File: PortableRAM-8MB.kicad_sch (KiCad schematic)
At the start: 34 parts, among them J1 RAM Connector, J2 JTAG_Header_2.54mm_1x06, U1 ATF1502ASL, U10 AMS1117-3.3, U11 74HC245, U12 74HC245, U2 IS61WV5128BLL-10TLI, U3 IS61WV5128BLL-10TLI, U4 IS61WV5128BLL-10TLI, U5 IS61WV5128BLL-10TLI, U6 IS61WV5128BLL-10TLI, U7 IS61WV5128BLL-10TLI, U8 IS61WV5128BLL-10TLI, U9 IS61WV5128BLL-10TLI

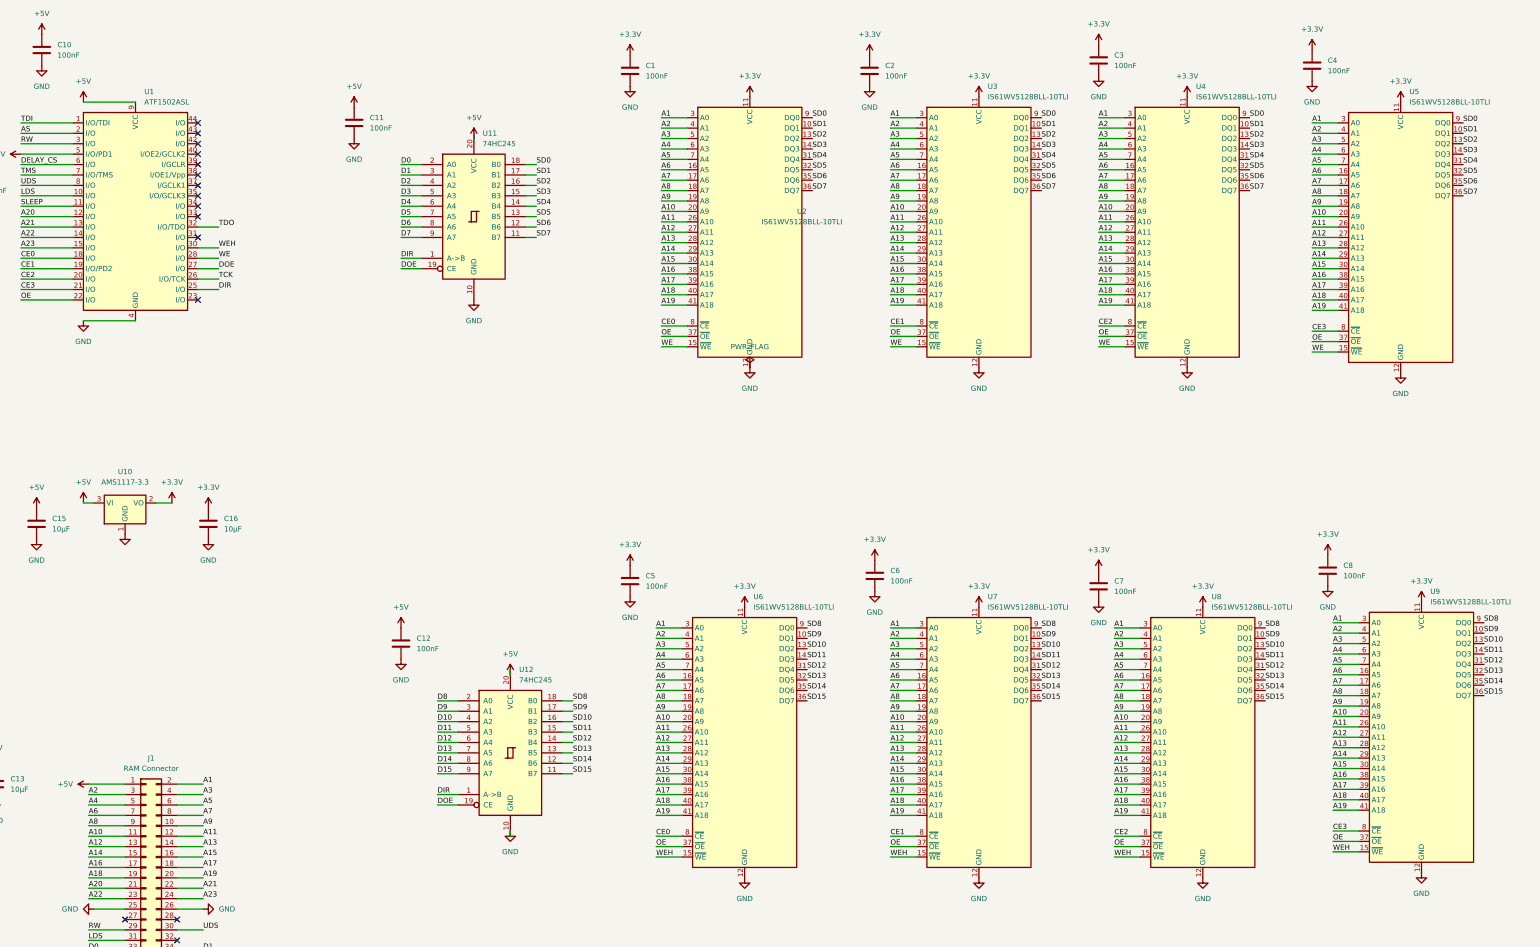
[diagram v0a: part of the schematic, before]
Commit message: Schematic: all-5V conversion + AS6C8008 (1Mx8) memory swap
- All +3.3V power symbols converted to +5V; AMS1117 LDO (U10) and its
  rail markers/stub wires removed — single 5V domain
- SRAM symbol renumbered in place to the AS6C8008 TSOP-II-44 pinout
  (graphics, wires, and labels untouched); pins 33/34 kept as VCC/GND
  rail ties (NC on the chip, preserves board plane stitching)
- New pins: A19 (18) labeled A19RAM on all 8 chips, driven by CPLD
  pin 33; CE2 (40) tied to +5V via power symbols
- PortableRAM.kicad_sym updated: AS6C8008 replaces IS61WV5128BLL
- ERC: no new issues vs v0.2 baseline (PWR_FLAG/VCC-alias warnings
  and prior exclusions remain)

Co-Authored-By: Claude Fable 5 <noreply@anthropic.com>
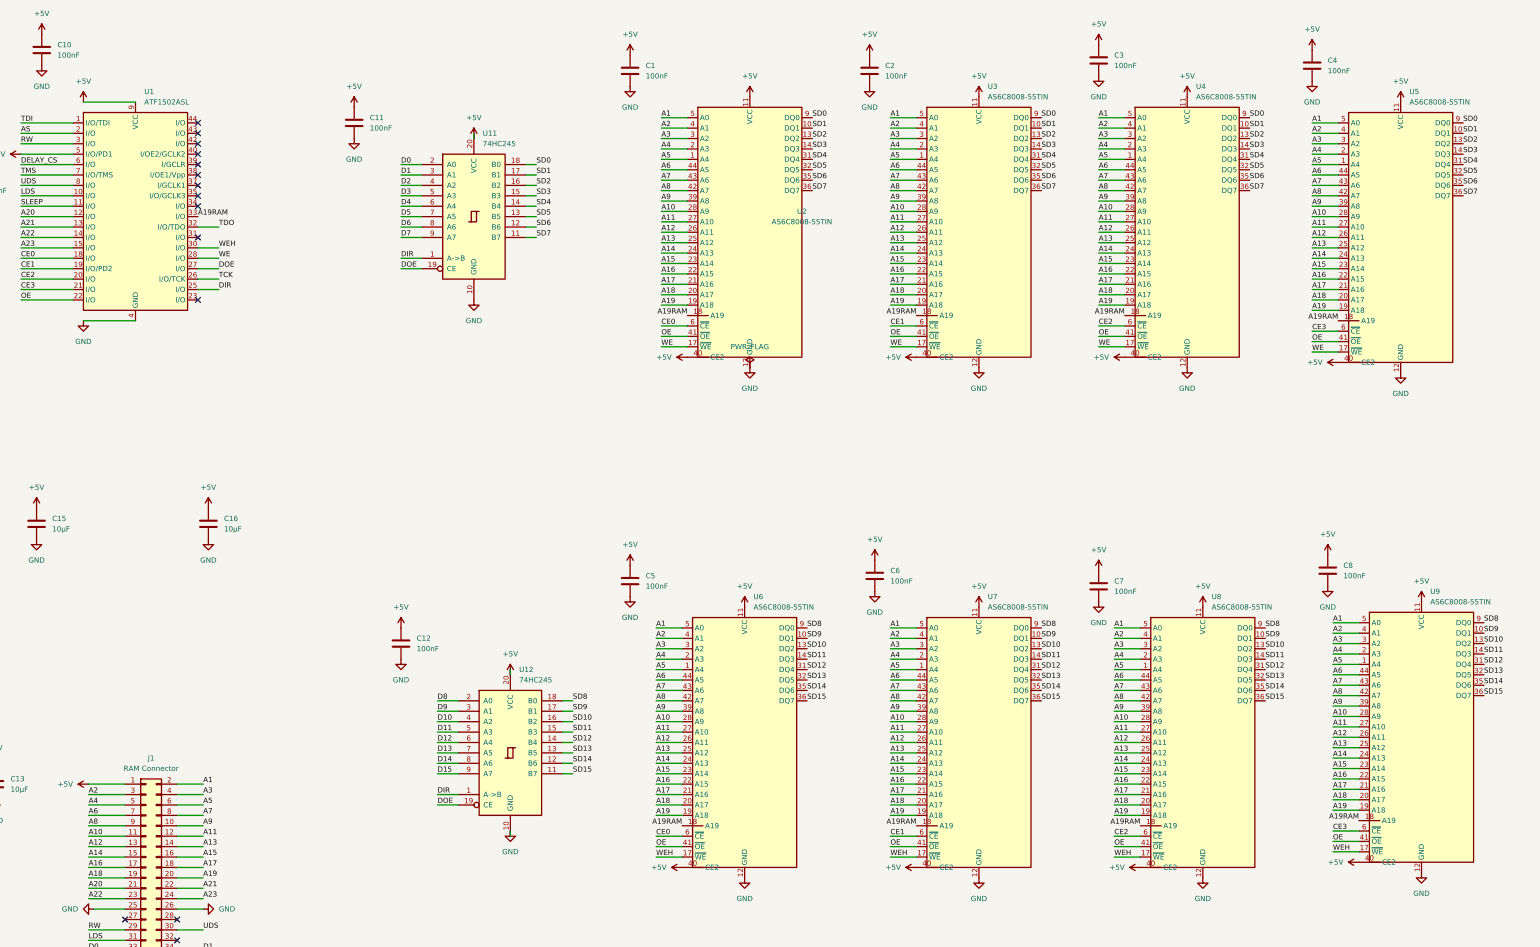
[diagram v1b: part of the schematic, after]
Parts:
- removed U10: AMS1117-3.3, Package_TO_SOT_SMD:SOT-223-3_TabPin2, symbol Regulator_Linear:AMS1117-3.3
- U2, U3, U4, U5, U6, U7, U8, U9: value IS61WV5128BLL-10TLI -> AS6C8008-55TIN; symbol PortableRAM:IS61WV5128BLL -> PortableRAM:AS6C8008
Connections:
- net +3.3V is gone; now on net +5V: C1.1, C16.1, C2.1, C3.1, C4.1, C5.1, C6.1, C7.1, C8.1, U2.11 (VCC), U2.33 (VCC), U3.11 (VCC), U3.33 (VCC), U4.11 (VCC), U4.33 (VCC), U5.11 (VCC), U5.33 (VCC), U6.11 (VCC), U6.33 (VCC), U7.11 (VCC), U7.33 (VCC), U8.11 (VCC), U8.33 (VCC), U9.11 (VCC), U9.33 (VCC)
- net +5V: now also U2.40 (CE2), U3.40 (CE2), U4.40 (CE2), U5.40 (CE2), U6.40 (CE2), U7.40 (CE2), U8.40 (CE2), U9.40 (CE2)
- net A1: now also U2.5 (A0), U3.5 (A0), U4.5 (A0), U5.5 (A0), U6.5 (A0), U7.5 (A0), U8.5 (A0), U9.5 (A0); no longer U2.3 (A0), U3.3 (A0), U4.3 (A0), U5.3 (A0), U6.3 (A0), U7.3 (A0), U8.3 (A0), U9.3 (A0)
- net A10: now also U2.28 (A9), U3.28 (A9), U4.28 (A9), U5.28 (A9), U6.28 (A9), U7.28 (A9), U8.28 (A9), U9.28 (A9); no longer U2.20 (A9), U3.20 (A9), U4.20 (A9), U5.20 (A9), U6.20 (A9), U7.20 (A9), U8.20 (A9), U9.20 (A9)
- net A11: now also U2.27 (A10), U3.27 (A10), U4.27 (A10), U5.27 (A10), U6.27 (A10), U7.27 (A10), U8.27 (A10), U9.27 (A10); no longer U2.26 (A10), U3.26 (A10), U4.26 (A10), U5.26 (A10), U6.26 (A10), U7.26 (A10), U8.26 (A10), U9.26 (A10)
- net A12: now also U2.26 (A11), U3.26 (A11), U4.26 (A11), U5.26 (A11), U6.26 (A11), U7.26 (A11), U8.26 (A11), U9.26 (A11); no longer U2.27 (A11), U3.27 (A11), U4.27 (A11), U5.27 (A11), U6.27 (A11), U7.27 (A11), U8.27 (A11), U9.27 (A11)
- net A13: now also U2.25 (A12), U3.25 (A12), U4.25 (A12), U5.25 (A12), U6.25 (A12), U7.25 (A12), U8.25 (A12), U9.25 (A12); no longer U2.28 (A12), U3.28 (A12), U4.28 (A12), U5.28 (A12), U6.28 (A12), U7.28 (A12), U8.28 (A12), U9.28 (A12)
- net A14: now also U2.24 (A13), U3.24 (A13), U4.24 (A13), U5.24 (A13), U6.24 (A13), U7.24 (A13), U8.24 (A13), U9.24 (A13); no longer U2.29 (A13), U3.29 (A13), U4.29 (A13), U5.29 (A13), U6.29 (A13), U7.29 (A13), U8.29 (A13), U9.29 (A13)
- net A15: now also U2.23 (A14), U3.23 (A14), U4.23 (A14), U5.23 (A14), U6.23 (A14), U7.23 (A14), U8.23 (A14), U9.23 (A14); no longer U2.30 (A14), U3.30 (A14), U4.30 (A14), U5.30 (A14), U6.30 (A14), U7.30 (A14), U8.30 (A14), U9.30 (A14)
- net A16: now also U2.22 (A15), U3.22 (A15), U4.22 (A15), U5.22 (A15), U6.22 (A15), U7.22 (A15), U8.22 (A15), U9.22 (A15); no longer U2.38 (A15), U3.38 (A15), U4.38 (A15), U5.38 (A15), U6.38 (A15), U7.38 (A15), U8.38 (A15), U9.38 (A15)
- net A17: now also U2.21 (A16), U3.21 (A16), U4.21 (A16), U5.21 (A16), U6.21 (A16), U7.21 (A16), U8.21 (A16), U9.21 (A16); no longer U2.39 (A16), U3.39 (A16), U4.39 (A16), U5.39 (A16), U6.39 (A16), U7.39 (A16), U8.39 (A16), U9.39 (A16)
- net A18: now also U2.20 (A17), U3.20 (A17), U4.20 (A17), U5.20 (A17), U6.20 (A17), U7.20 (A17), U8.20 (A17), U9.20 (A17); no longer U2.40 (A17), U3.40 (A17), U4.40 (A17), U5.40 (A17), U6.40 (A17), U7.40 (A17), U8.40 (A17), U9.40 (A17)
- net A19: now also U2.19 (A18), U3.19 (A18), U4.19 (A18), U5.19 (A18), U6.19 (A18), U7.19 (A18), U8.19 (A18), U9.19 (A18); no longer U2.41 (A18), U3.41 (A18), U4.41 (A18), U5.41 (A18), U6.41 (A18), U7.41 (A18), U8.41 (A18), U9.41 (A18)
- net A3: now also U2.3 (A2), U3.3 (A2), U4.3 (A2), U5.3 (A2), U6.3 (A2), U7.3 (A2), U8.3 (A2), U9.3 (A2); no longer U2.5 (A2), U3.5 (A2), U4.5 (A2), U5.5 (A2), U6.5 (A2), U7.5 (A2), U8.5 (A2), U9.5 (A2)
- net A4: now also U2.2 (A3), U3.2 (A3), U4.2 (A3), U5.2 (A3), U6.2 (A3), U7.2 (A3), U8.2 (A3), U9.2 (A3); no longer U2.6 (A3), U3.6 (A3), U4.6 (A3), U5.6 (A3), U6.6 (A3), U7.6 (A3), U8.6 (A3), U9.6 (A3)
- net A5: now also U2.1 (A4), U3.1 (A4), U4.1 (A4), U5.1 (A4), U6.1 (A4), U7.1 (A4), U8.1 (A4), U9.1 (A4); no longer U2.7 (A4), U3.7 (A4), U4.7 (A4), U5.7 (A4), U6.7 (A4), U7.7 (A4), U8.7 (A4), U9.7 (A4)
- net A6: now also U2.44 (A5), U3.44 (A5), U4.44 (A5), U5.44 (A5), U6.44 (A5), U7.44 (A5), U8.44 (A5), U9.44 (A5); no longer U2.16 (A5), U3.16 (A5), U4.16 (A5), U5.16 (A5), U6.16 (A5), U7.16 (A5), U8.16 (A5), U9.16 (A5)
- net A7: now also U2.43 (A6), U3.43 (A6), U4.43 (A6), U5.43 (A6), U6.43 (A6), U7.43 (A6), U8.43 (A6), U9.43 (A6); no longer U2.17 (A6), U3.17 (A6), U4.17 (A6), U5.17 (A6), U6.17 (A6), U7.17 (A6), U8.17 (A6), U9.17 (A6)
- net A8: now also U2.42 (A7), U3.42 (A7), U4.42 (A7), U5.42 (A7), U6.42 (A7), U7.42 (A7), U8.42 (A7), U9.42 (A7); no longer U2.18 (A7), U3.18 (A7), U4.18 (A7), U5.18 (A7), U6.18 (A7), U7.18 (A7), U8.18 (A7), U9.18 (A7)
- net A9: now also U2.39 (A8), U3.39 (A8), U4.39 (A8), U5.39 (A8), U6.39 (A8), U7.39 (A8), U8.39 (A8), U9.39 (A8); no longer U2.19 (A8), U3.19 (A8), U4.19 (A8), U5.19 (A8), U6.19 (A8), U7.19 (A8), U8.19 (A8), U9.19 (A8)
- net CE0: now also U2.6 (~{CE}), U6.6 (~{CE}); no longer U2.8 (~{CE}), U6.8 (~{CE})
- net CE1: now also U3.6 (~{CE}), U7.6 (~{CE}); no longer U3.8 (~{CE}), U7.8 (~{CE})
- net CE2: now also U4.6 (~{CE}), U8.6 (~{CE}); no longer U4.8 (~{CE}), U8.8 (~{CE})
- net CE3: now also U5.6 (~{CE}), U9.6 (~{CE}); no longer U5.8 (~{CE}), U9.8 (~{CE})
- net OE: now also U2.41 (~{OE}), U3.41 (~{OE}), U4.41 (~{OE}), U5.41 (~{OE}), U6.41 (~{OE}), U7.41 (~{OE}), U8.41 (~{OE}), U9.41 (~{OE}); no longer U2.37 (~{OE}), U3.37 (~{OE}), U4.37 (~{OE}), U5.37 (~{OE}), U6.37 (~{OE}), U7.37 (~{OE}), U8.37 (~{OE}), U9.37 (~{OE})
- net WE: now also U2.17 (~{WE}), U3.17 (~{WE}), U4.17 (~{WE}), U5.17 (~{WE}); no longer U2.15 (~{WE}), U3.15 (~{WE}), U4.15 (~{WE}), U5.15 (~{WE})
- net WEH: now also U6.17 (~{WE}), U7.17 (~{WE}), U8.17 (~{WE}), U9.17 (~{WE}); no longer U6.15 (~{WE}), U7.15 (~{WE}), U8.15 (~{WE}), U9.15 (~{WE})
- net A19RAM: now reaches U1.33 (I/O)
- net A19RAM: now also U2.18 (A19), U3.18 (A19), U4.18 (A19), U5.18 (A19), U6.18 (A19), U7.18 (A19), U8.18 (A19), U9.18 (A19)
- no-connect marks 15 -> 14

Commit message: Add SIZE jumper: one board, 4MB or 8MB by population
- JP1 (1x02 header) + R5 10K pull-up on CPLD pin 34 (SIZE8), placed in
  the old LDO area; project-local Jumper_1x02 symbol added to library
- Firmware: banks 2-3 and their address window gated by SIZE8 — jumper
  open = 8MB (8 chips), closed = 4MB (populate U2/U3/U6/U7, banks 0-1).
  Unpopulated space is never decoded, keeping the Mac's boot-time RAM
  sizing away from floating-bus false positives
- Verified WE split intact after the AS6C8008 renumbering: /WE -> pin 28
  + U2-U5 pad 17, /WEH -> pin 30 + U6-U9 pad 17; firmware gates writes
  per byte lane (WEL&LDS / WEH&UDS)
- ERC: 0 errors

Co-Authored-By: Claude Fable 5 <noreply@anthropic.com>
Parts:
- added JP1: SIZE: open=8MB closed=4MB, Connector_PinHeader_2.54mm:PinHeader_1x02_P2.54mm_Vertical, symbol PortableRAM:Jumper_1x02
- added R5: 10K, Resistor_SMD:R_0805_2012Metric, symbol Device:R
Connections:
- net +5V: now also R5.1
- net GND: now also JP1.2 (Pin_2)
- net SIZE8: now reaches U1.34 (I/O)
- net SIZE8: now also JP1.1 (Pin_1), R5.2
- net WE renamed WEL
- no-connect marks 14 -> 13
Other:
- title: Mac Portable 4MB RAM Card -> Mac Portable 4or8MB RAM Card
- moved on the sheet: C1, C10, C15, C16, C2, C3, C4, C5, C6, C7, C8, C9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

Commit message: Rename A19RAM -> BANKSEL
Clearer name for the CPLD-computed signal (= !A20) that selects which
1MB half of each 2MB bank is active; avoids visual collision with the
Mac /A19 address net on the schematic.

Co-Authored-By: Claude Fable 5 <noreply@anthropic.com>
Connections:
- net A19RAM renamed BANKSEL
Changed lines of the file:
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@@
 		)
 	)
-	(label "A19RAM"
+	(label "BANKSEL"
 		(at 220.98 90.17 0)
 		(effects
@@
 		)
 	)
-	(label "A19RAM"
+	(label "BANKSEL"
 		(at 450.85 238.76 180)
 		(effects
@@
 		)
 	)
-	(label "A19RAM"
+	(label "BANKSEL"
 		(at 396.24 114.3 180)
 		(effects
@@
 		)
 	)
-	(label "A19RAM"
+	(label "BANKSEL"
 		(at 499.11 115.57 180)
 		(effects
@@
 		)
 	)
-	(label "A19RAM"
+	(label "BANKSEL"
 		(at 447.04 114.3 180)
 		(effects
@@
 		)
 	)
-	(label "A19RAM"
+	(label "BANKSEL"
 		(at 396.24 238.76 180)
 		(effects
@@
 		)
 	)
-	(label "A19RAM"
+	(label "BANKSEL"
 		(at 339.09 238.76 180)
 		(effects
@@
 		)
 	)
-	(label "A19RAM"
+	(label "BANKSEL"
 		(at 340.36 114.3 180)
 		(effects
@@
 		)
 	)
-	(label "A19RAM"
+	(label "BANKSEL"
 		(at 504.19 237.49 180)
 		(effects

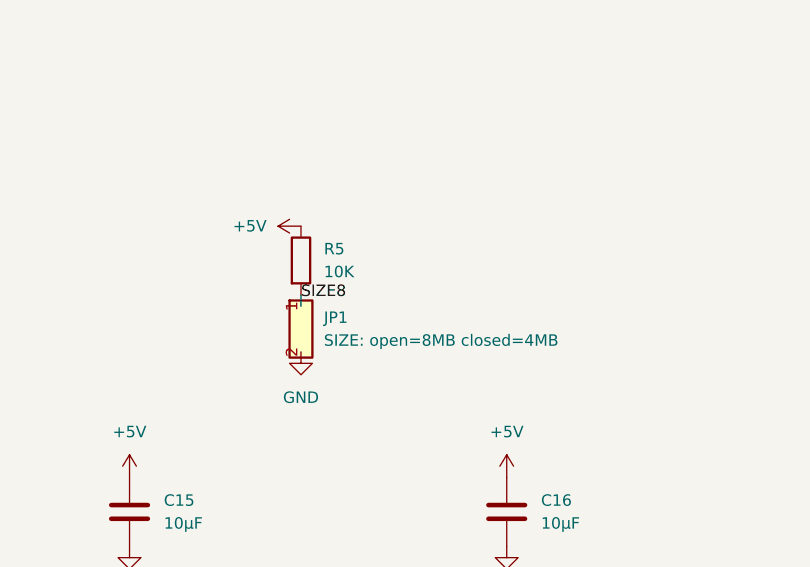
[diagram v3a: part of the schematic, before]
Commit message: Add C18 (100nF, 4th CPLD VCC pin) and C19 (10uF, power-entry bulk)
Decoupling now: one 100nF per AS6C8008 (8) + one per ATF1502 VCC pin (4)
+ one per 74HC245 (2) = 14, plus 5x 10uF bulk. C19 kept at 10uF to match
purchased stock. Place C19 adjacent to J1 VCC pins at layout time.

Co-Authored-By: Claude Fable 5 <noreply@anthropic.com>
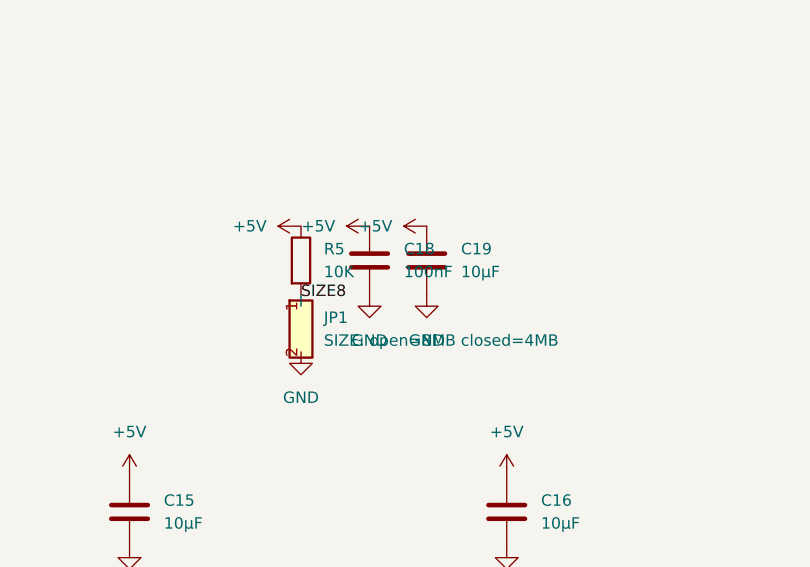
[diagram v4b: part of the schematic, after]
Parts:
- added C18: 100nF, Capacitor_SMD:C_0805_2012Metric, symbol Device:C
- added C19: 10µF, Capacitor_SMD:C_0805_2012Metric, symbol Device:C
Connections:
- net +5V: now also C18.1, C19.1
- net GND: now also C18.2, C19.2
